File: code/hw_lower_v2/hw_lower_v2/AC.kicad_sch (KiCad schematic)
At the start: 38 parts, among them K1 AHES4191, Q1 BSS138, Q2 BSS138, Q3 BSS138, T1 TS3193-2C 2mA/2mA, U1 BRCS02C, U2 BL0942

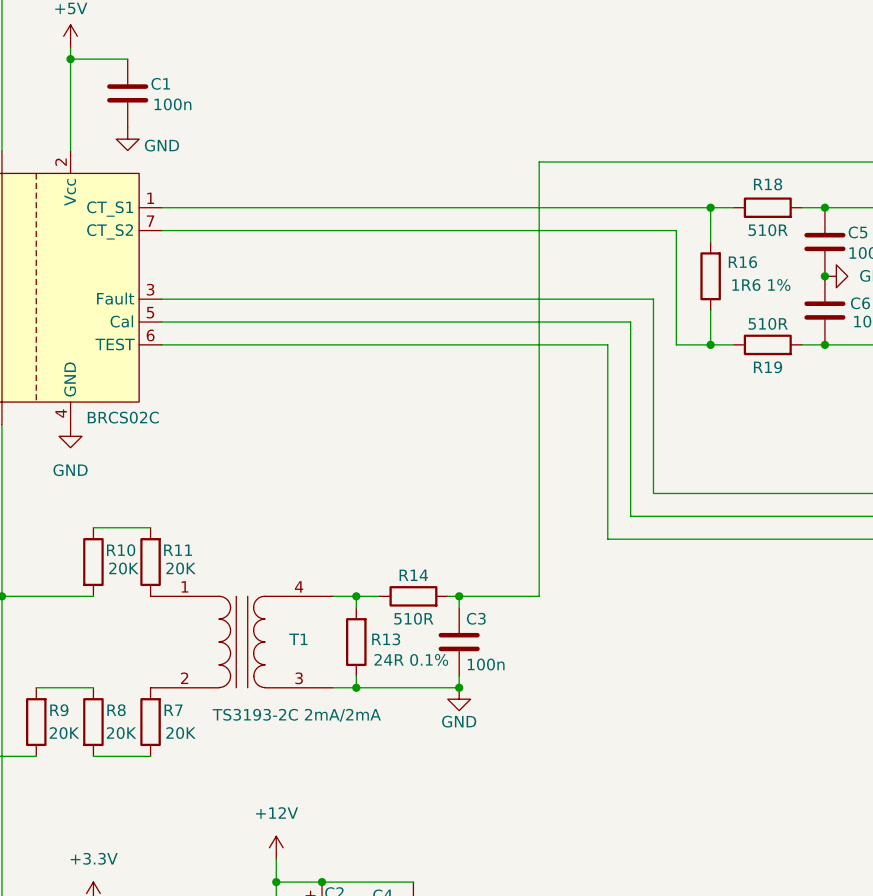
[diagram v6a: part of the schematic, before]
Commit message: made a full reposition of the whole pcb. When I get everything working, the milkv module can be on the bottom pcb and all the device specific devices can be on the other pcb. Also now conceptualy, the current board can be broken onto two, and be made into a thin long one
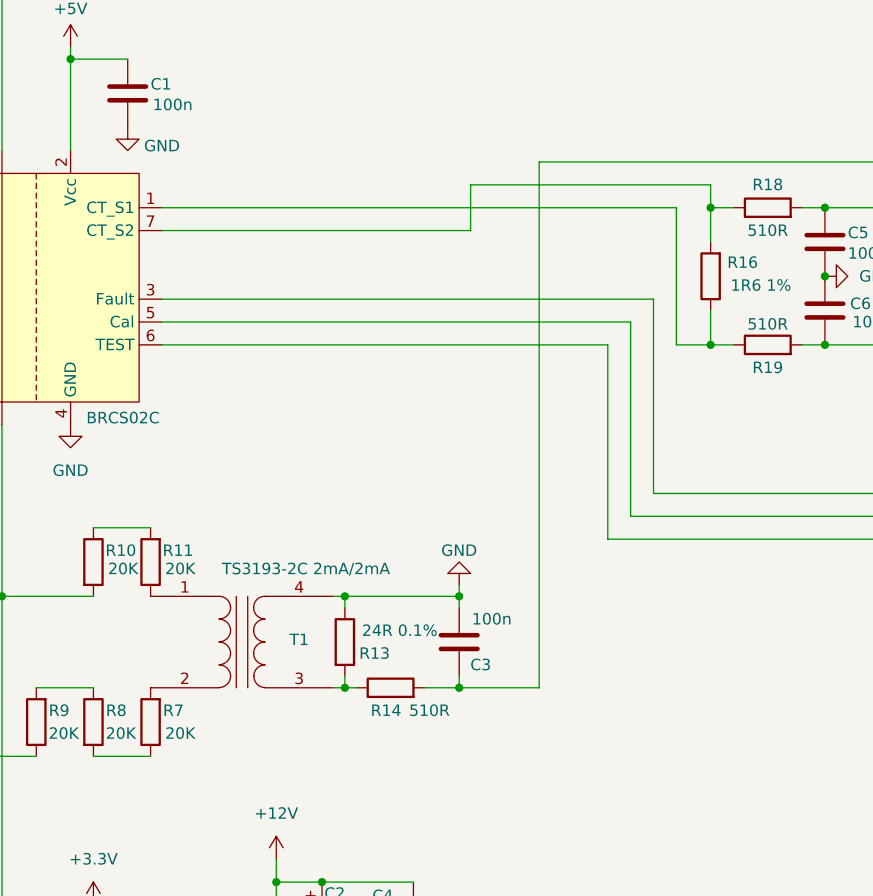
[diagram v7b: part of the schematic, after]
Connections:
- net GND: now also T1.4 (SB); no longer T1.3 (SA)
- net at R13.2, R14.1: now also T1.3 (SA); no longer T1.4 (SB)
- net at R16.1, R19.1: now also U1.1 (CT_S1); no longer U1.7 (CT_S2)
- net at R16.2, R18.1: now also U1.7 (CT_S2); no longer U1.1 (CT_S1)
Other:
- moved on the sheet: C3, R13, R14

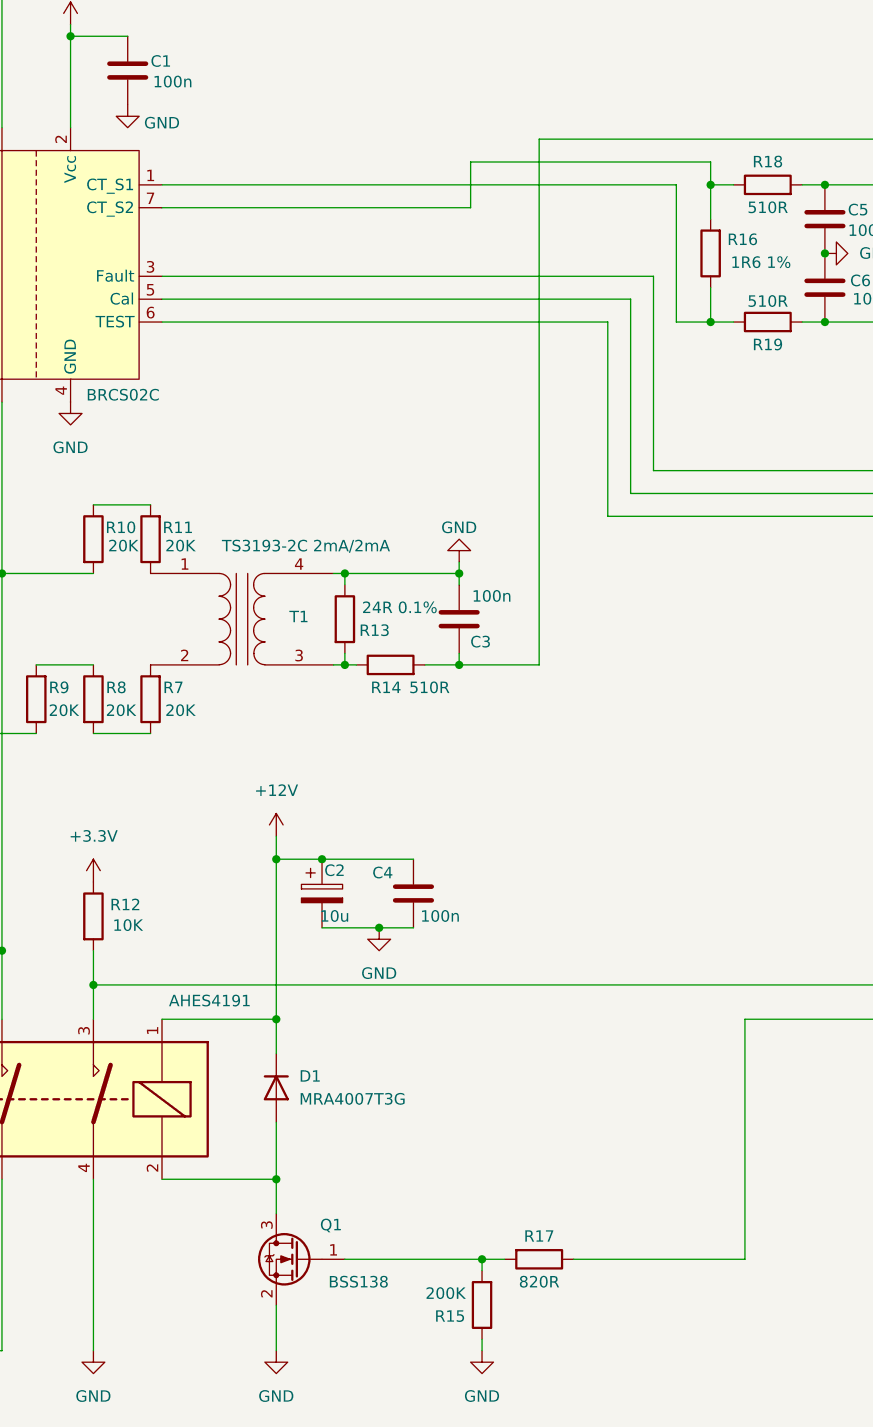
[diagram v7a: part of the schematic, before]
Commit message: add JLCPCB tooling holes and simplify further
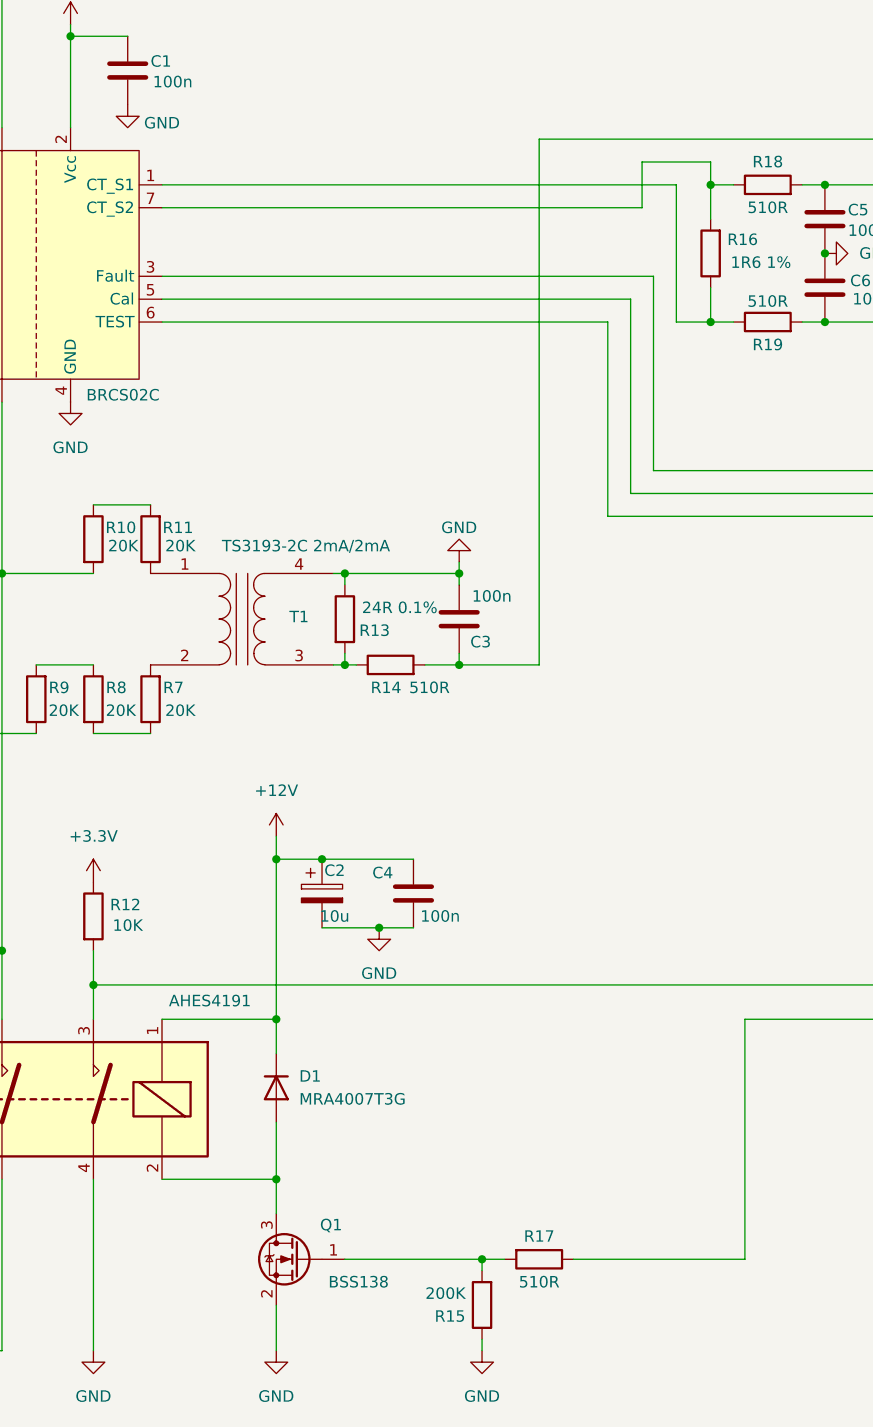
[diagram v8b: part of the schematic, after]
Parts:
- R17: value 820R -> 510R; LCSC C23253 -> C23193
- R26: footprint Resistor_SMD:R_0603_1608Metric -> Resistor_SMD:R_1206_3216Metric
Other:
- title: EVSE -> BlueEVSE
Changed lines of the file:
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@@
 	(paper "A4")
 	(title_block
-		(title "EVSE")
+		(title "BlueEVSE")
 		(date "2024-07-14")
 		(rev "V2")
@@
 	(wire
 		(pts
-			(xy 118.11 57.15) (xy 118.11 52.07)
+			(xy 137.16 57.15) (xy 137.16 52.07)
 		)
 		(stroke
@@
 	(wire
 		(pts
-			(xy 118.11 52.07) (xy 144.78 52.07)
+			(xy 137.16 52.07) (xy 144.78 52.07)
 		)
 		(stroke
@@
 	(wire
 		(pts
-			(xy 83.82 57.15) (xy 118.11 57.15)
+			(xy 83.82 57.15) (xy 137.16 57.15)
 		)
 		(stroke
@@
 			)
 		)
-		(property "Value" "820R"
+		(property "Value" "510R"
 			(at 125.73 176.53 90)
 			(effects
@@
 			)
 		)
-		(property "LCSC" "C23253"
+		(property "LCSC" "C23193"
 			(at 125.73 173.99 0)
 			(effects
@@
 			)
 		)
-		(property "Footprint" "Resistor_SMD:R_0603_1608Metric"
+		(property "Footprint" "Resistor_SMD:R_1206_3216Metric"
 			(at 222.758 91.44 90)
 			(effects
